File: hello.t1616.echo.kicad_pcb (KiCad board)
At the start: 2 copper layers, 51.4 x 25.4 mm, 10 parts, among them J1 Conn_01x03_Male, J2 Conn_FTDI_01x06_Male, SW1 BUTTON_B3SN, U1 ATtiny1616-S

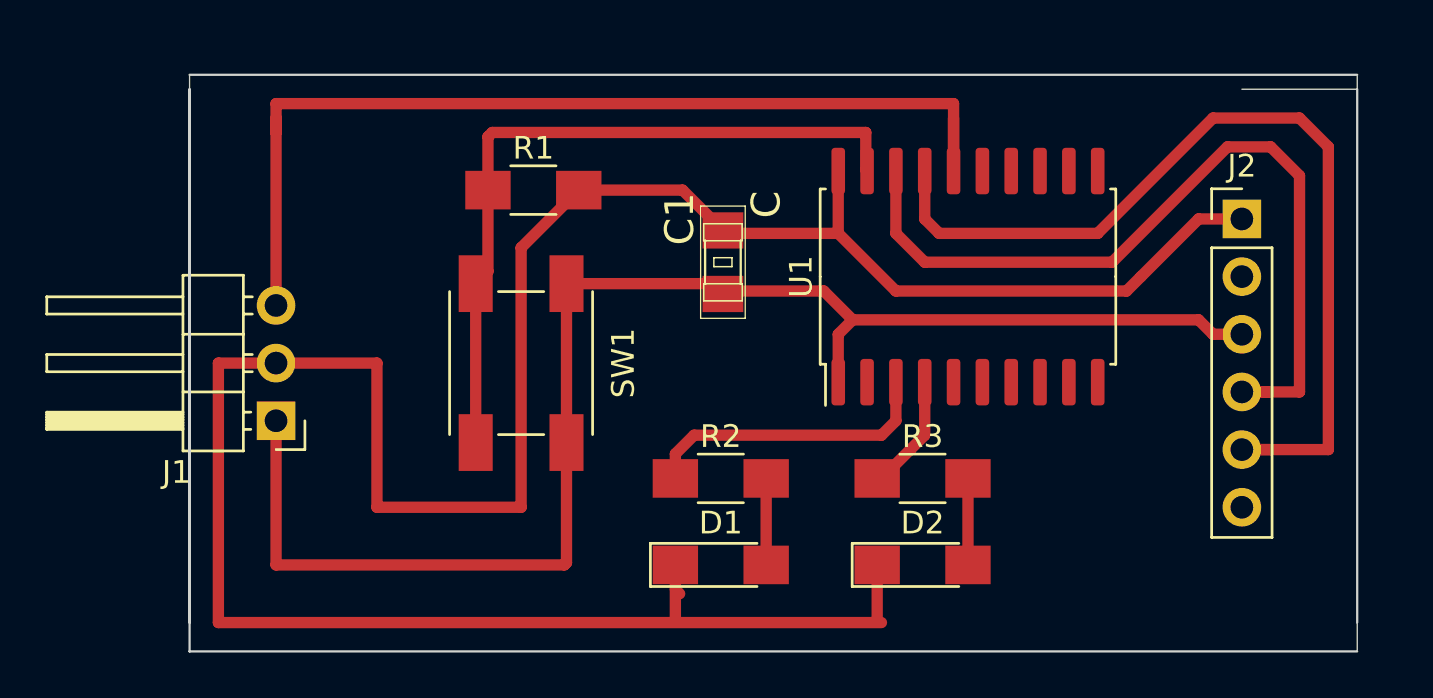
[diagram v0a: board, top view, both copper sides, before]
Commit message: Moved serial lines to correct pins.
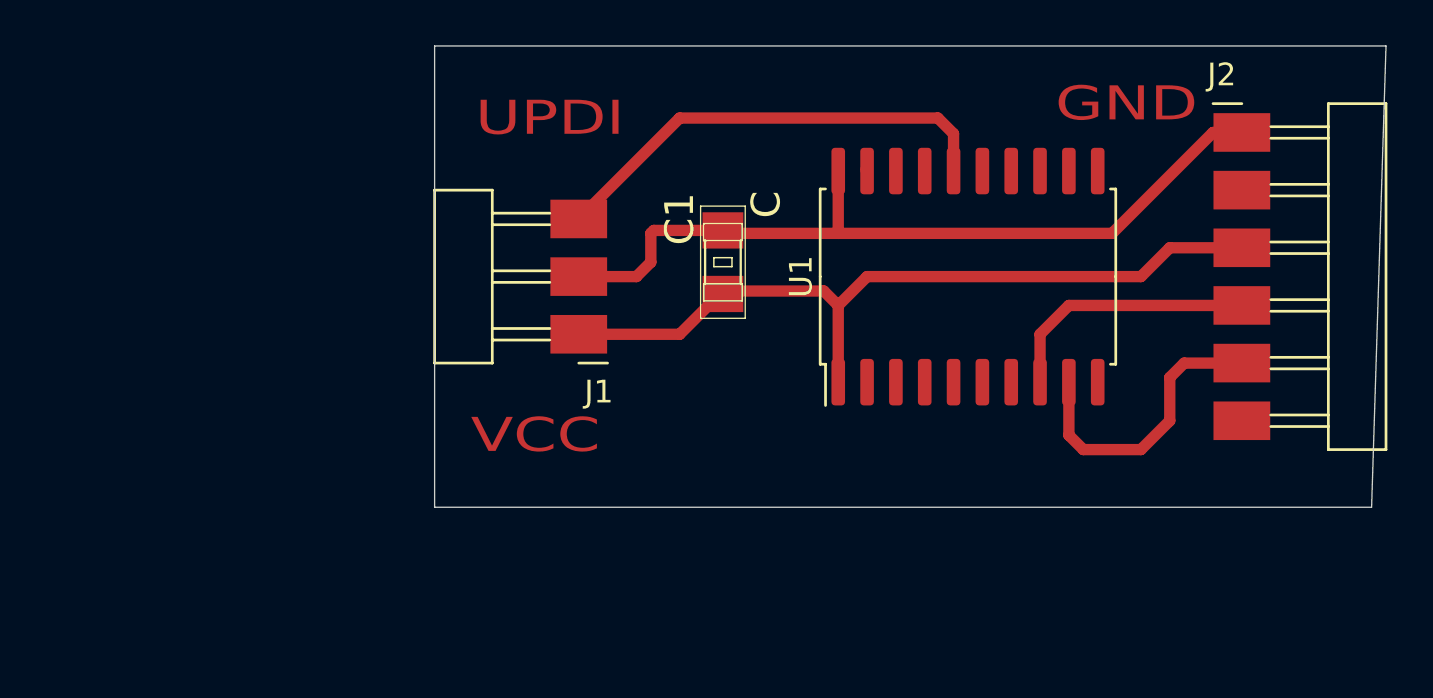
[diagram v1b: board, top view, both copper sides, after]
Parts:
- removed D1: LED YLW, fab:LED_1206
- removed D2: LED GRN, fab:LED_1206
- removed R1, R2, R3: 1K, fab:R_1206
- removed SW1: BUTTON_B3SN, fab:Button_Omron_B3SN_6x6mm
- J1: footprint Connector_PinHeader_2.54mm:PinHeader_1x03_P2.54mm_Horizontal -> fab:Header_SMD_01x03_P2.54mm_Horizontal_Male
- J2: footprint Connector_PinHeader_2.54mm:PinHeader_1x06_P2.54mm_Vertical -> fab:Header_SMD_01x06_P2.54mm_Horizontal_Male
- moved J1 13.9 mm to (128.9, 120.7)
- moved J2 3.81 mm to (158.1, 111.8)
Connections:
- J2 pad 2: Net-(J2-Pad2) -> (no net)
- J2 pad 6: Net-(J2-Pad6) -> (no net)
- U1 pad 10: Net-(U1-Pad10) -> (no net)
- U1 pad 11: Net-(U1-Pad11) -> (no net)
- U1 pad 12: Net-(U1-Pad12) -> (no net)
- U1 pad 13: Net-(U1-Pad13) -> (no net)
- U1 pad 14: Net-(U1-Pad14) -> (no net)
- U1 pad 15: Net-(U1-Pad15) -> (no net)
- U1 pad 17: RX -> (no net)
- U1 pad 18: TX -> (no net)
- U1 pad 19: Net-(R1-Pad1) -> (no net)
- U1 pad 2: Net-(U1-Pad2) -> (no net)
- U1 pad 3: LED1 -> (no net)
- U1 pad 4: LED2 -> (no net)
- U1 pad 5: Net-(U1-Pad5) -> (no net)
- U1 pad 6: Net-(U1-Pad6) -> (no net)
- U1 pad 7: Net-(U1-Pad7) -> (no net)
- U1 pad 8: Net-(U1-Pad8) -> TX
- U1 pad 9: Net-(U1-Pad9) -> RX
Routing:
- net GND: track 115.4 -> 35.4 mm
- net VCC: track 70.7 -> 35.3 mm
- net Net-(R1-Pad1): track 32.1 -> 0.00 mm
- net RX: track 40.6 -> 12.9 mm
- net TX: track 36.4 -> 11.5 mm
- net Net-(J1-Pad3): track 44.0 -> 20.3 mm
- net LED1: track 13.1 -> 0.00 mm
- net LED2: track 5.22 -> 0.00 mm
- net Net-(D2-Pad2): track 3.81 -> 0.00 mm
- net Net-(D1-Pad2): track 3.81 -> 0.00 mm
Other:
- board size 51.4 x 25.4 mm -> 41.9 x 20.3 mm
- board text added: "GND"
- board text added: "UPDI"
- board text added: "VCC"

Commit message: Added thruhole version
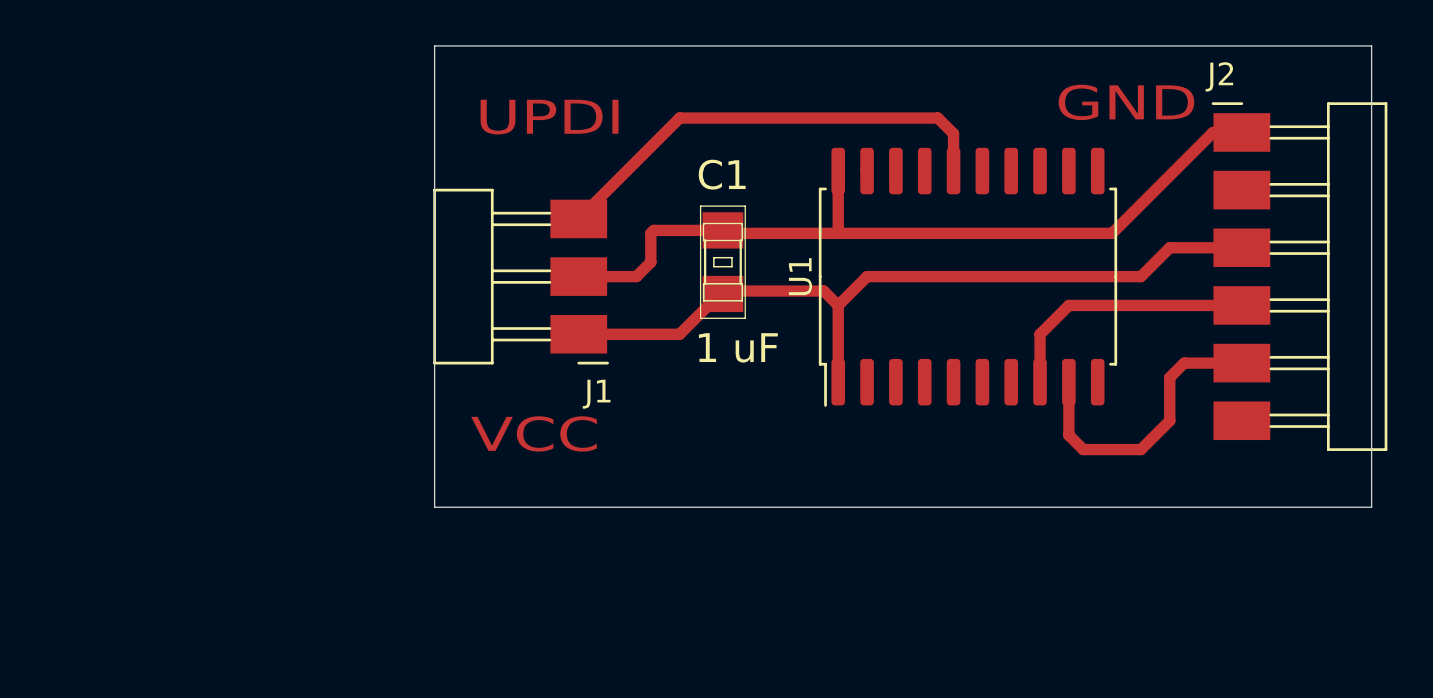
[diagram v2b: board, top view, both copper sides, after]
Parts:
- C1: value C -> 1 uF
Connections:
- J2 pad 2: (no net) -> Net-(J2-Pad2)
- J2 pad 6: (no net) -> Net-(J2-Pad6)
- U1 pad 10: (no net) -> Net-(U1-Pad10)
- U1 pad 11: (no net) -> Net-(U1-Pad11)
- U1 pad 12: (no net) -> Net-(U1-Pad12)
- U1 pad 13: (no net) -> Net-(U1-Pad13)
- U1 pad 14: (no net) -> Net-(U1-Pad14)
- U1 pad 15: (no net) -> Net-(U1-Pad15)
- U1 pad 17: (no net) -> Net-(U1-Pad17)
- U1 pad 18: (no net) -> Net-(U1-Pad18)
- U1 pad 19: (no net) -> Net-(U1-Pad19)
- U1 pad 2: (no net) -> Net-(U1-Pad2)
- U1 pad 3: (no net) -> Net-(U1-Pad3)
- U1 pad 4: (no net) -> Net-(U1-Pad4)
- U1 pad 5: (no net) -> Net-(U1-Pad5)
- U1 pad 6: (no net) -> Net-(U1-Pad6)
- U1 pad 7: (no net) -> Net-(U1-Pad7)
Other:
- board size 41.9 x 20.3 mm -> 41.3 x 20.3 mm
